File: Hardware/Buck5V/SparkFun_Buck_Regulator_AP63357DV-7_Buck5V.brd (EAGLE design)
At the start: 25.4 x 25.4 mm, 52 parts, among them J3 POWER_JACK, U1 AP63357

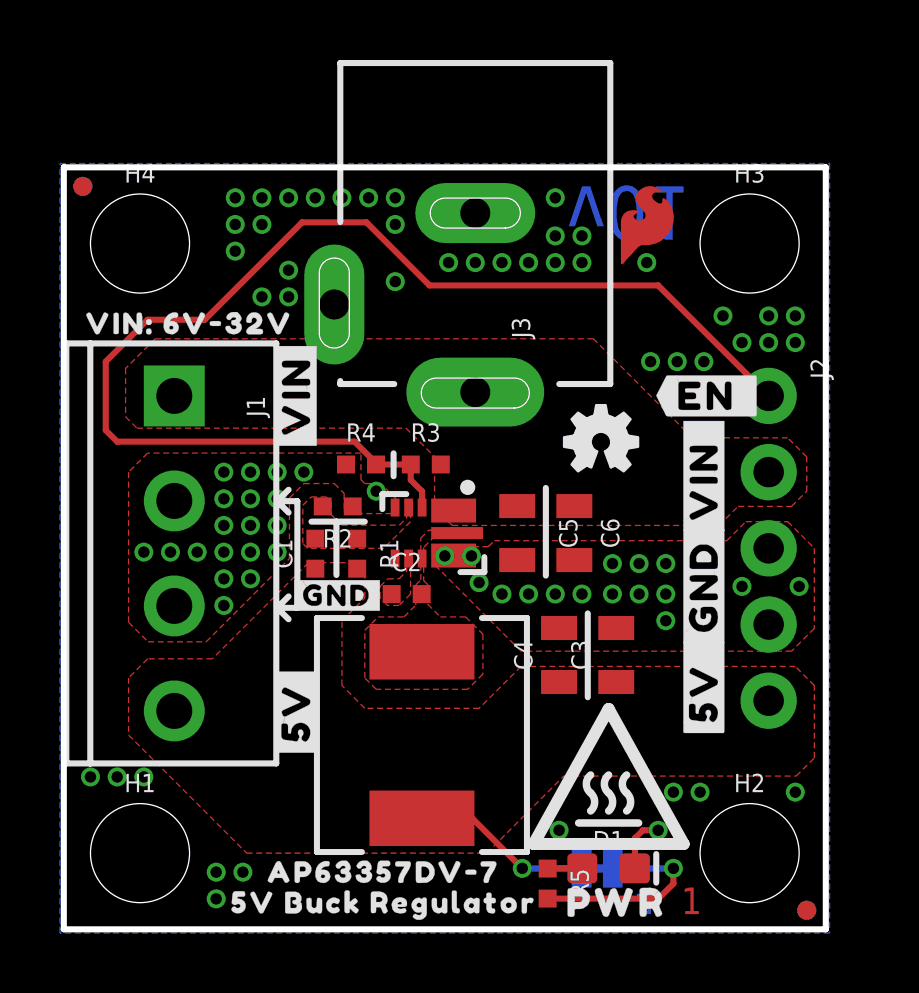
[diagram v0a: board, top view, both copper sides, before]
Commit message: v01 changes implemented.
Schematic:
Add note for LED jumper
Add green wire for EN
Section titles center anchor
Rename Regulator section
Layout:
Increase selective solder width
Move 1x1 thermal pad
Make silk labels more explicit
Add "CAUTION: HOT" or just "HOT" silk
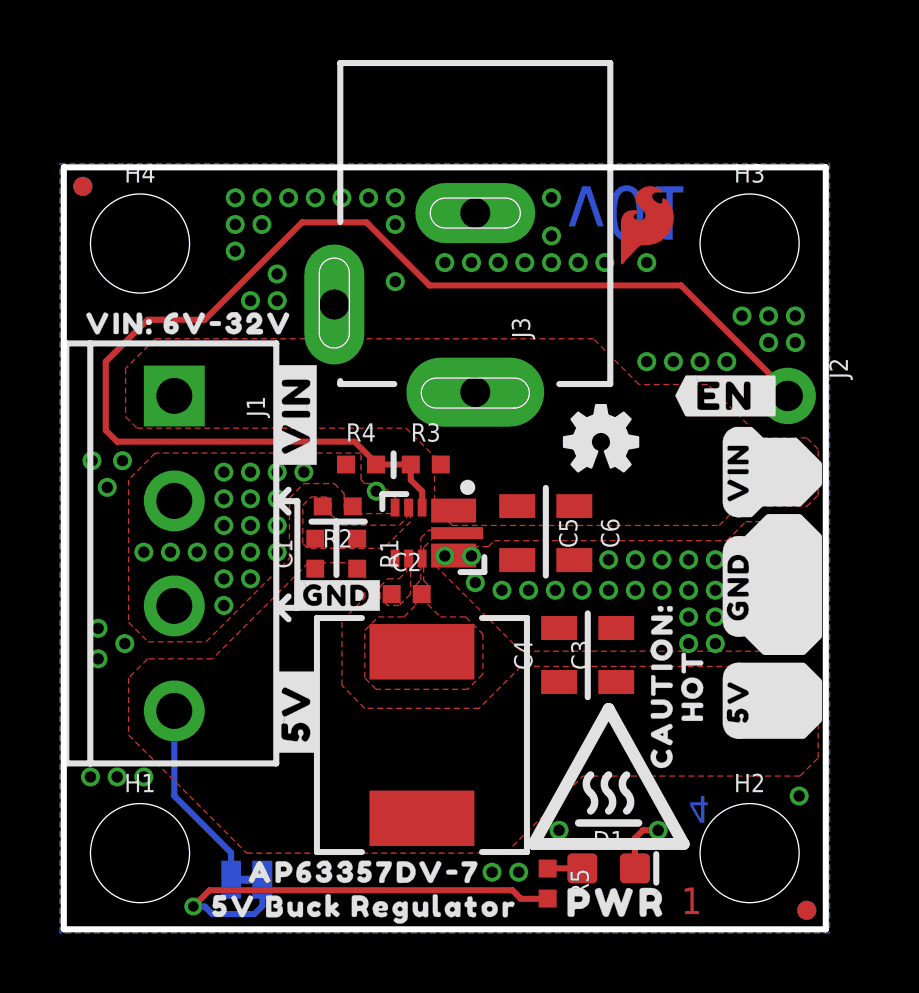
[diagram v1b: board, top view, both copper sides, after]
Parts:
- removed U$12: (no value), output:#_5V_#6
- added U$24: (no value), output:#5V#0
- added U$25: (no value), output:HOT0
- added U$26: (no value), output:#VIN#3
- U$10: device output:#GND#0 -> output:#5V#10
- U$11: device output:#GND#0 -> output:6V#32V10
- U$14: device output:#_GND_#6 -> output:#5V#0
- U$16: device output:#_5V_#6 -> output:CAUTION#0
- U$3: device output:#VIN#0 -> output:#5V#4
- U$4: device output:#5V#0 -> output:#VIN#8
- U$5: device output:#5V_#0 -> output:#VIN#0
- U$6: device output:#VIN_#0 -> output:#GND#0
- U$9: device output:#VIN#0 -> output:#GND#9
- moved U$4 12.2 mm to (1.52, 17.8), flipped to the bottom, turned to 270 degrees
- moved PWR 11.7 mm to (6.10, 1.65)
- moved U$3 10.5 mm to (7.75, 7.24)
- moved U$11 9.70 mm to (8.00, 17.8), turned to 180 degrees
- moved U$15 8.88 mm to (6.10, 4.57), turned to 270 degrees
- moved U$5 7.27 mm to (22.5, 15.2)
- moved U$10 6.99 mm to (1.52, 7.24)
- moved U$9 5.21 mm to (1.52, 12.6)
- moved U$14 3.86 mm to (22.5, 7.62)
- moved U$6 3.86 mm to (22.5, 11.4)
- moved U$16 1.53 mm to (19.9, 8.13), flipped to the top, turned to 90 degrees
- moved U$13 1.15 mm to (22.5, 15.2)
- moved U$7 1.14 mm to (22.5, 11.4), flipped to the bottom, turned to 270 degrees
- moved U$2 0.65 mm to (10.0, 0.76)
- moved U$19 0.64 mm to (22.2, 17.8)
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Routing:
- net N$5: track 6.93 -> 15.5 mm
- net EN: track 41.0 -> 41.7 mm
- net 5V: track 6.01 -> 6.41 mm, vias 1 -> 0
- net GND: vias 81 -> 91

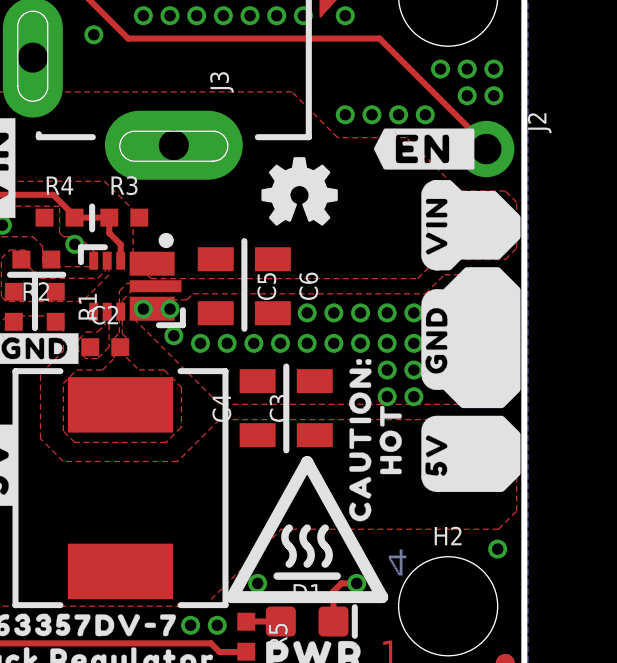
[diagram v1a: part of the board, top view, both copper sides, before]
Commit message: Slight component shuffling in prep for protos.
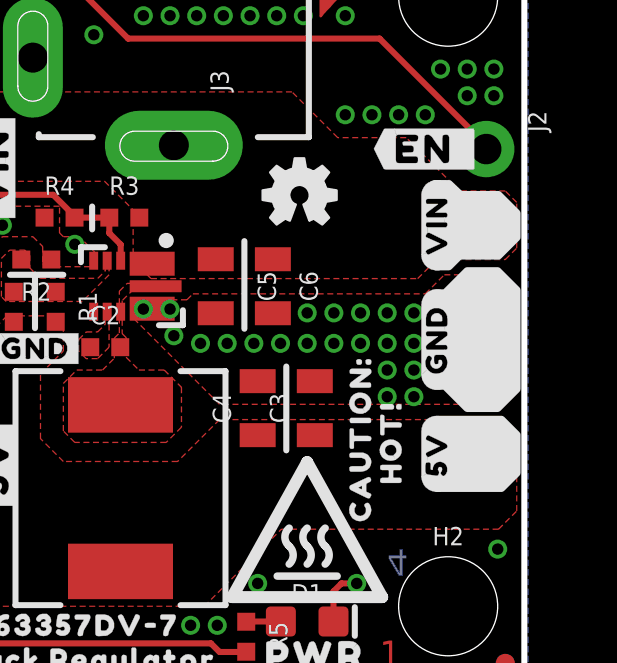
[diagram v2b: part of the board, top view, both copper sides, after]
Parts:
- removed U$25: (no value), output:HOT0
- added U$12: (no value), output:HOT##0
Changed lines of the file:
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@@
 <vertex x="25.146" y="13.081"/>
 <vertex x="25.146" y="9.779"/>
-<vertex x="24.638" y="9.271"/>
-<vertex x="23.368" y="9.271"/>
+<vertex x="24.5084625" y="9.1414625"/>
+<vertex x="23.4975375" y="9.1414625"/>
 </polygon>
 <polygon width="0.254" layer="21">
@@
 <vertex x="22.88896875" y="16.619053125"/>
 <vertex x="23.26979375" y="16.256"/>
-<vertex x="24.384" y="16.256"/>
-<vertex x="25.146" y="15.494"/>
-<vertex x="25.146" y="14.859"/>
-<vertex x="24.511" y="14.224"/>
+<vertex x="24.533859375" y="16.256"/>
+<vertex x="25.146" y="15.643859375"/>
+<vertex x="25.146" y="14.8336"/>
+<vertex x="24.5364" y="14.224"/>
 <vertex x="23.241" y="14.224"/>
 <vertex x="22.88031875" y="13.86331875"/>
@@
 </polygon>
 <polygon width="0.2032" layer="22">
-<vertex x="2.105659375" y="14.424659375"/>
-<vertex x="3.175" y="15.494"/>
-<vertex x="4.191" y="15.494"/>
+<vertex x="2.032" y="14.351"/>
+<vertex x="3.048" y="15.367"/>
+<vertex x="4.318" y="15.367"/>
 <vertex x="4.953" y="14.732"/>
 <vertex x="4.953" y="10.287"/>
 <vertex x="4.191" y="9.525"/>
-<vertex x="3.302" y="9.525"/>
-<vertex x="2.105659375" y="10.721340625"/>
+<vertex x="3.29438125" y="9.525"/>
+<vertex x="2.02438125" y="10.795"/>
+<vertex x="2.159" y="10.795"/>
+<vertex x="2.159" y="14.351"/>
 </polygon>
 <polygon width="0.2032" layer="22">
@@
 <polygon width="0.254" layer="22">
 <vertex x="22.418040625" y="13.858240625"/>
-<vertex x="22.86" y="13.86078125"/>
-<vertex x="23.241" y="14.224"/>
-<vertex x="24.511" y="14.224"/>
-<vertex x="25.146" y="14.859"/>
-<vertex x="25.146" y="15.621"/>
-<vertex x="24.511" y="16.256"/>
-<vertex x="23.241" y="16.256"/>
-<vertex x="22.86" y="16.637"/>
-<vertex x="22.4561375" y="16.621759375"/>
+<vertex x="22.864165625" y="13.86080625"/>
+<vertex x="23.245140625" y="14.224"/>
+<vertex x="24.5364" y="14.224"/>
+<vertex x="25.146" y="14.8336"/>
+<vertex x="25.146" y="15.651478125"/>
+<vertex x="24.541478125" y="16.256"/>
+<vertex x="23.268940625" y="16.256"/>
+<vertex x="22.8854" y="16.621759375"/>
+<vertex x="22.4536" y="16.621759375"/>
 <vertex x="22.4561375" y="16.383"/>
 <vertex x="22.987" y="16.383"/>
@@
 <vertex x="22.4663" y="9.883140625"/>
 <vertex x="22.755859375" y="9.883140625"/>
-<vertex x="23.368" y="9.271"/>
-<vertex x="24.638" y="9.271"/>
+<vertex x="23.495" y="9.144"/>
+<vertex x="24.511" y="9.144"/>
 <vertex x="25.146" y="9.779"/>
 <vertex x="25.146" y="13.081"/>
@@
 <element name="U$14" library="output" package="#5V#0" value="" x="22.479" y="7.62" smashed="yes" rot="MR270"/>
 <element name="U$16" library="output" package="CAUTION#0" value="" x="19.939" y="8.128" smashed="yes" rot="R90"/>
-<element name="U$25" library="output" package="HOT0" value="" x="20.955" y="8.128" smashed="yes" rot="R90"/>
 <element name="U$26" library="output" package="#VIN#3" value="" x="7.747" y="17.145" smashed="yes" rot="R90"/>
 <element name="U$3" library="output" package="#5V#4" value="" x="7.747" y="7.239" smashed="yes" rot="R90"/>
@@
 <element name="U$10" library="output" package="#5V#10" value="" x="1.524" y="7.239" smashed="yes" rot="MR270"/>
 <element name="U$11" library="output" package="6V#32V10" value="" x="8.001" y="17.78" smashed="yes" rot="MR180"/>
+<element name="U$12" library="output" package="HOT##0" value="" x="20.955" y="8.001" smashed="yes" rot="R90"/>
 </elements>
 <signals>

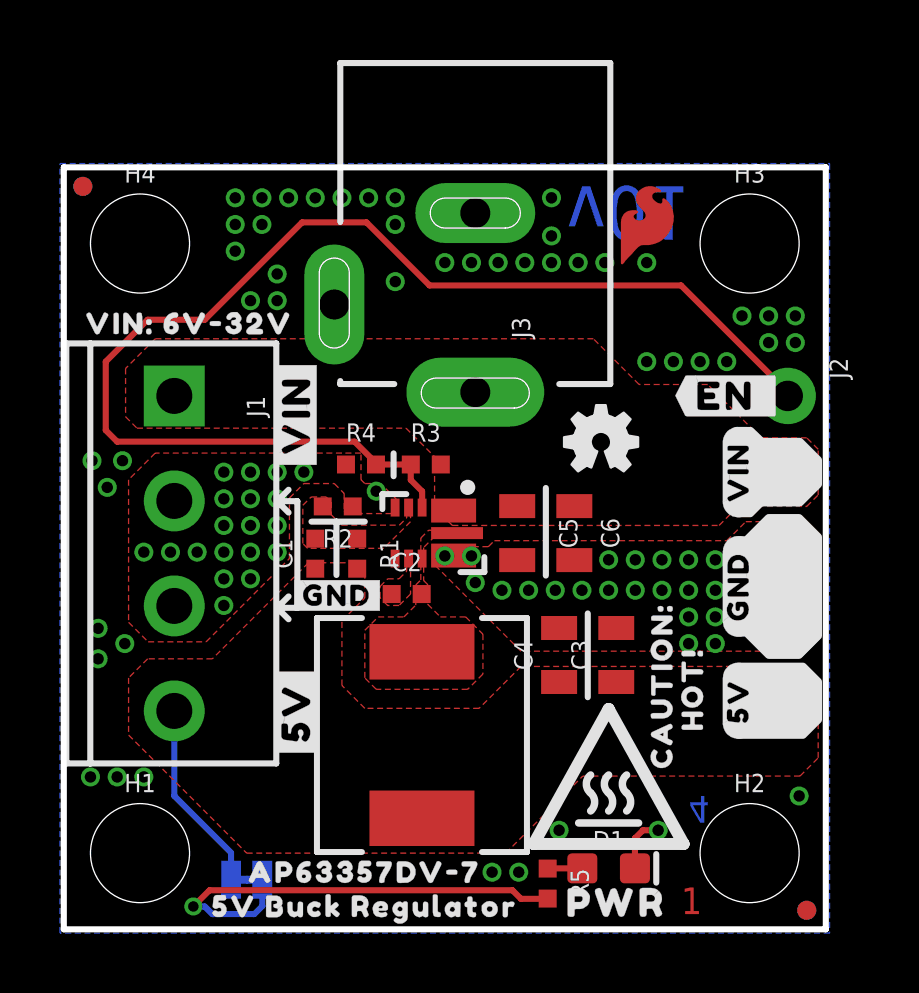
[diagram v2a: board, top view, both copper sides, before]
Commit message: Remove silk from Power Jack so no silk overhangs.
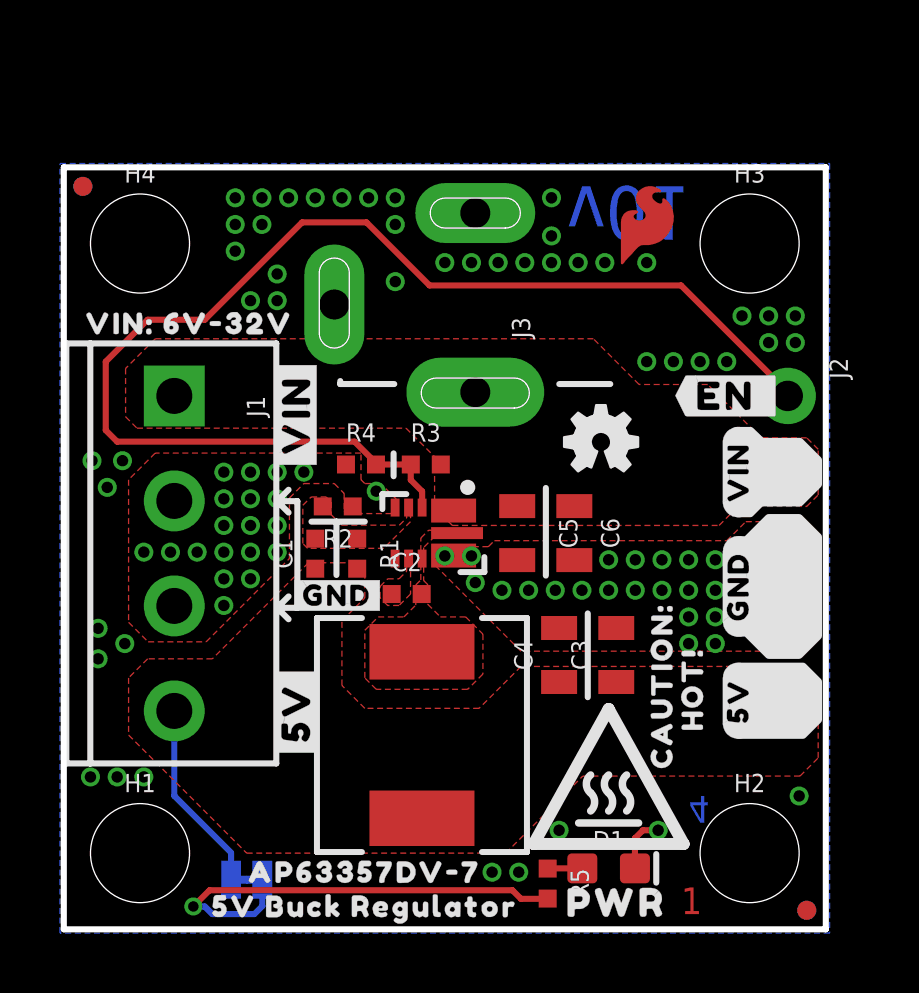
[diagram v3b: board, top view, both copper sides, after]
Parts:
- J3: device SparkFun-Connectors:POWER_JACK_PTH_SLOT -> SparkFun-Connectors:POWER_JACK_PTH_SLOT_NO_OVRHNG_SILK
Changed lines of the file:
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@@
 <attribute name="VALUE" x="1.397" y="17.78" size="0.6096" layer="27" font="vector" ratio="20" rot="R270"/>
 </element>
-<element name="J3" library="SparkFun-Connectors" package="POWER_JACK_PTH_SLOT" value="POWER_JACK" x="13.716" y="23.876" smashed="yes" rot="R90">
+<element name="J3" library="SparkFun-Connectors" package="POWER_JACK_PTH_SLOT_NO_OVRHNG_SILK" value="POWER_JACK" x="13.716" y="23.876" smashed="yes" rot="R90">
 <attribute name="NAME" x="15.546" y="19.703" size="0.6096" layer="25" font="vector" ratio="20" rot="R90"/>
-<attribute name="PROD_ID" value="CONN-08197" x="22.606" y="23.876" size="1.778" layer="27" rot="R90" display="off"/>
 <attribute name="VALUE" x="16.573" y="19.603" size="0.6096" layer="27" font="vector" ratio="20" rot="R90"/>
 </element>
